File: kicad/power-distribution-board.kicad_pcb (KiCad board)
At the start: 2 copper layers, 0 parts

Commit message: Adding pcb layout
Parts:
- added D1: LED, LED_THT:LED_D5.0mm, F.Cu at (126.5, 82.0)
- added D2: LED, LED_THT:LED_D5.0mm, F.Cu at (149.0, 82.0)
- added D3: 1N4001, Rumblesan_Standard_Parts:D_DO-41_SOD81_P10.16mm_Horizontal, F.Cu at (82.2, 96.7)
- added D4: 1N4001, Rumblesan_Standard_Parts:D_DO-41_SOD81_P10.16mm_Horizontal, F.Cu at (96.3, 96.7)
- added G***: LOGO, Rumblesan_Panel_Graphics:Logo_Ammonite-simple_small_10.4mmx12.0mm, F.Cu at (144.0, 105.0)
- added H1: MountingHole_Pad, MountingHole:MountingHole_3.2mm_M3_DIN965_Pad, F.Cu at (73.0, 74.0)
- added H2: MountingHole_Pad, MountingHole:MountingHole_3.2mm_M3_DIN965_Pad, F.Cu at (73.0, 121.0)
- added H3: MountingHole_Pad, MountingHole:MountingHole_3.2mm_M3_DIN965_Pad, F.Cu at (195.0, 74.0)
- added H4: MountingHole_Pad, MountingHole:MountingHole_3.2mm_M3_DIN965_Pad, F.Cu at (195.0, 121.0)
- added J1: Banana Socket PCBMount, Rumblesan_Audio_Connectors:Deltron_571_PCB_BananaJack, F.Cu at (83.3, 74.7)
- added J10: Banana Socket PCBMount, Rumblesan_Audio_Connectors:Deltron_571_PCB_BananaJack, F.Cu at (194.3, 93.3)
- added J11: Conn_01x04, Connector_Molex:Molex_KK-396_5273-04A_1x04_P3.96mm_Vertical, F.Cu at (175.0, 118.0)
- added J2: Banana Socket PCBMount, Rumblesan_Audio_Connectors:Deltron_571_PCB_BananaJack, F.Cu at (105.3, 74.7)
- added J3: Banana Socket PCBMount, Rumblesan_Audio_Connectors:Deltron_571_PCB_BananaJack, F.Cu at (94.3, 74.7)
- added J4: Conn_02x08_Odd_Even, Rumblesan_Eurorack_Power:Eurorack_Power_IDC-Header_2x08_P2.54mm_Vertical, F.Cu at (114.8, 119.0)
- added J5: Conn_02x05_Odd_Even, Rumblesan_Eurorack_Power:Eurorack_Power_IDC-Header_2x05_P2.54mm_Vertical, F.Cu at (86.5, 119.0)
- added J6: 4U_Power, Rumblesan_4U_Power:4u_Power_Molex_KK-254_22-27-2041_1x04_P2.54mm_Vertical, F.Cu at (145.2, 119.0)
- added J7: Conn_01x03, Connector_Molex:Molex_KK-254_AE-6410-03A_1x03_P2.54mm_Vertical, F.Cu at (161.0, 119.0)
- added J8: Banana Socket PCBMount, Rumblesan_Audio_Connectors:Deltron_571_PCB_BananaJack, F.Cu at (194.3, 83.3)
- added J9: Banana Socket PCBMount, Rumblesan_Audio_Connectors:Deltron_571_PCB_BananaJack, F.Cu at (194.3, 103.3)
- added R1: 2k2, Rumblesan_Standard_Parts:R_Axial_DIN0207_L6.3mm_D2.5mm_P10.16mm_Horizontal, F.Cu at (122.0, 82.0)
- added R2: 2k2, Rumblesan_Standard_Parts:R_Axial_DIN0207_L6.3mm_D2.5mm_P10.16mm_Horizontal, F.Cu at (156.0, 82.0)
- added SW1: SW_DPDT_x2, Rumblesan_Standard_Parts:SW_DPDT_DailyWell_MiniToggle, F.Cu at (139.0, 82.0)
- added TP1: TestPoint, Rumblesan_Standard_Parts:TestPoint_Loop_D2.50mm_Drill1.0mm_LowProfile, F.Cu at (128.9, 96.0)
- added TP2: TestPoint, Rumblesan_Standard_Parts:TestPoint_Loop_D2.50mm_Drill1.0mm_LowProfile, F.Cu at (149.0, 96.0)
- added TP3: TestPoint, Rumblesan_Standard_Parts:TestPoint_Loop_D2.50mm_Drill1.0mm_LowProfile, F.Cu at (139.0, 96.0)
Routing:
- net -12V: track 0.00 -> 200.8 mm
- net +12V: track 0.00 -> 189.8 mm
- net Net-(D3-K): track 0.00 -> 77.1 mm
- net Net-(D4-A): track 0.00 -> 60.0 mm
- net Net-(D2-A): track 0.00 -> 4.46 mm
- net Net-(D1-K): track 0.00 -> 4.46 mm
- added copper zone on B.Cu, net GND
- added copper zone on F.Cu, net GND
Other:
- board outline added: 130 x 55 mm
- board text added: "+V"
- board text added: "-V"
- board text added: "GND"
- board text added: "OFF"
- board text added: "ON"

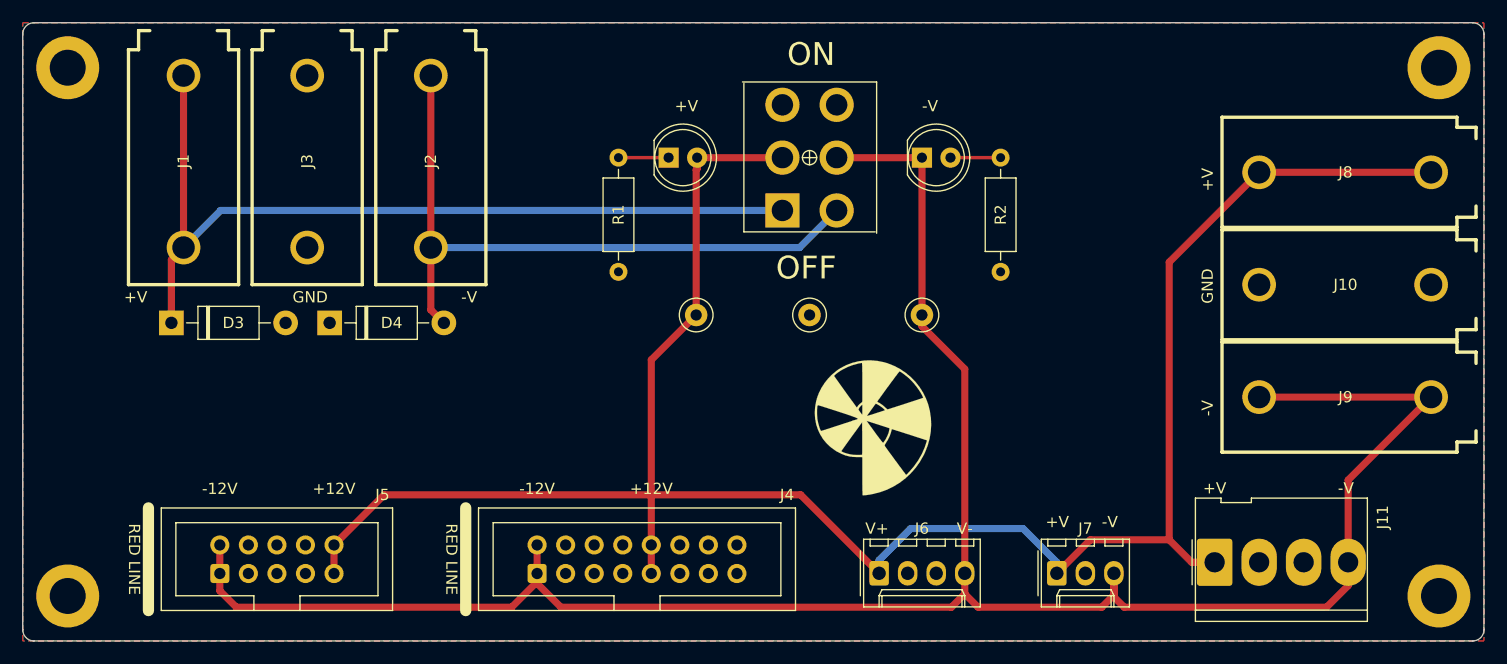
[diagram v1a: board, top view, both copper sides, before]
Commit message: Tweaking layout and adding silkscreen text
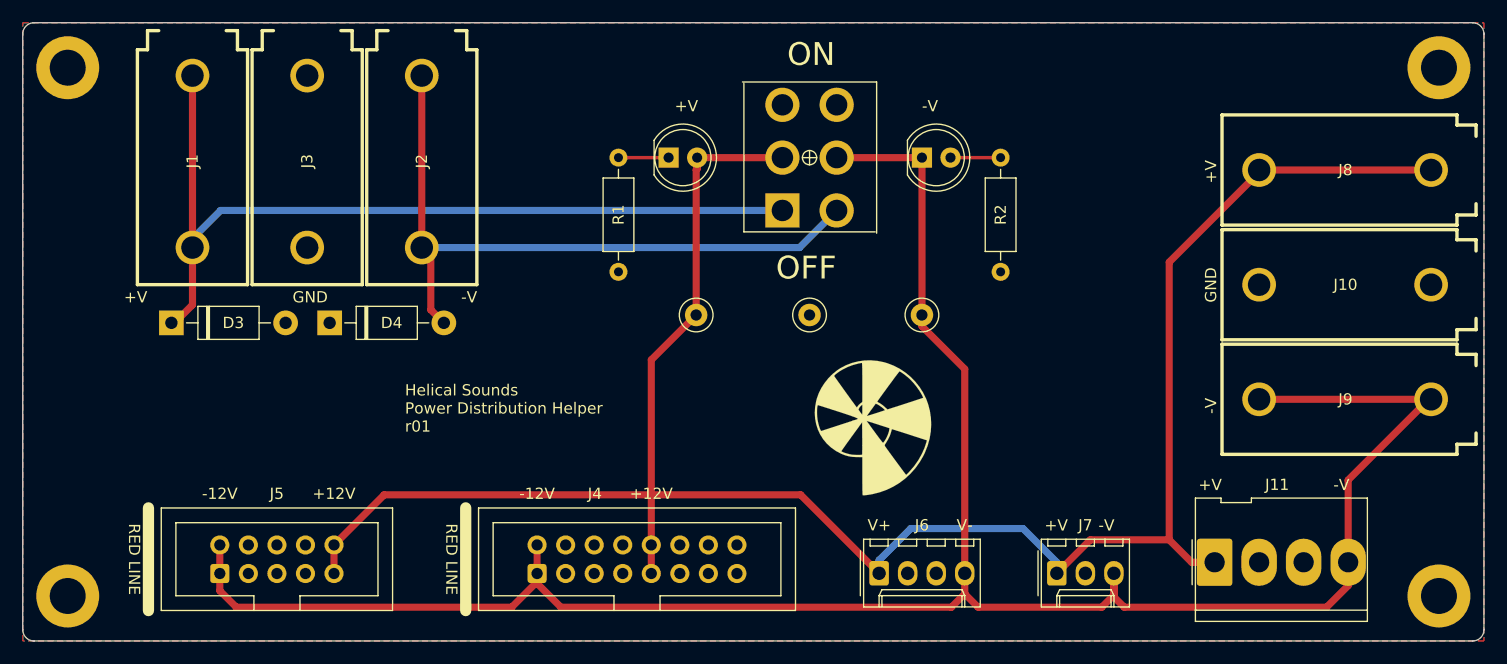
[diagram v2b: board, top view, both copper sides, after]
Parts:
- moved J2 0.81 mm to (104.5, 74.7)
- moved J1 0.79 mm to (84.1, 74.7)
- moved J8 0.21 mm to (194.3, 83.1)
- moved J9 0.19 mm to (194.3, 103.5)
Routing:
- net Net-(D4-A): track 60.0 -> 61.1 mm
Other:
- board text added: "${COMPANY} ${TITLE} ${REVISION}"
